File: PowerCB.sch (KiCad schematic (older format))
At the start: 16 parts, among them J1 USB_B_Micro, J2 Mounting_1, J3 Mounting_2, J6 Conn_01x02_Male, J7 Conn_01x02_Male, J8 Conn_01x02_Male, J9 Conn_01x02_Male, U1 TPS73633DBV

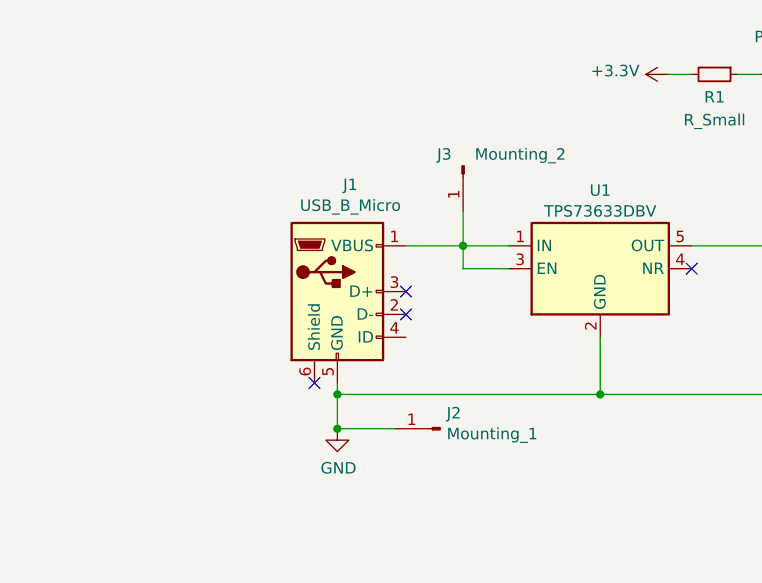
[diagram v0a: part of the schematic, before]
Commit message: feat: USB-C instead of Micro-USB connector
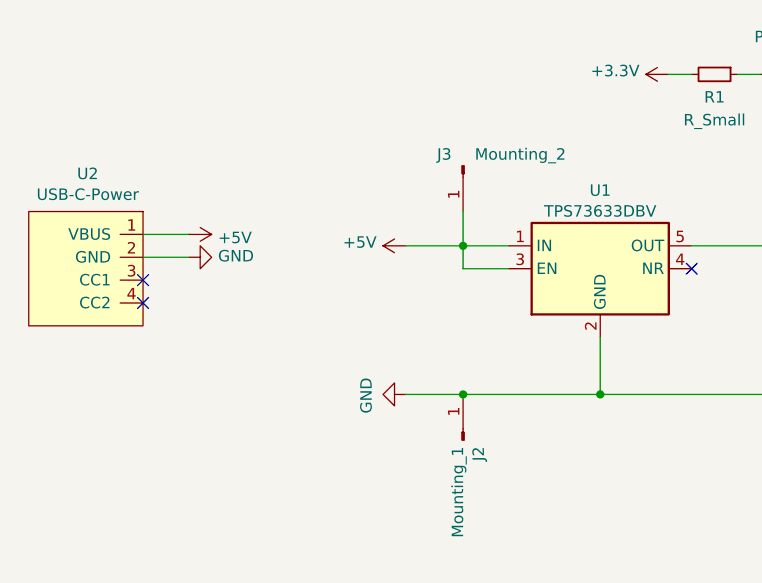
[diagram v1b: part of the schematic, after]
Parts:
- removed J1: USB_B_Micro, Connector_USB:USB_Micro-B_Amphenol_10103594-0001LF_Horizontal, symbol Connector:USB_B_Micro
- added U2: USB-C-Power, PowerCB:UJC-HP-3-SMT-TR, symbol PowerCB:USB-C-Power
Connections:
- net GND: now also U2.2 (GND)
- net +5V: now reaches J3.1 (Pin_1), U1.1 (IN), U1.3 (EN)
- net +5V: now also U2.1 (VBUS)
- no-connect marks 4 -> 3
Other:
- moved on the sheet: J2
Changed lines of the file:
@@
 EESchema Schematic File Version 4
-LIBS:PowerCB-cache
 EELAYER 30 0
 EELAYER END
@@
 Sheet 1 1
 Title "PowerCB"
-Date "2019-12-01"
-Rev "1.0"
+Date "2020-12-11"
+Rev "02"
 Comp ""
 Comment1 "https://creativecommons.org/licenses/by/4.0/"
@@
 Wire Wire Line
 	2800 2050 3000 2050
-NoConn ~ 2550 2250
-NoConn ~ 2550 2350
-Wire Wire Line
-	2250 2650 2250 2700
 $Comp
 L Device:LED D1
@@
 	4400 1300 4500 1300
 Wire Wire Line
-	3400 2700 2250 2700
-Wire Wire Line
 	3400 2450 3400 2700
-Connection ~ 2250 2700
-$Comp
-L Connector:USB_B_Micro J1
-U 1 1 5DA6372D
-P 2250 2250
-F 0 "J1" H 2307 2717 50  0000 C CNN
-F 1 "USB_B_Micro" H 2307 2626 50  0000 C CNN
-F 2 "Connector_USB:USB_Micro-B_Amphenol_10103594-0001LF_Horizontal" H 2400 2200 50  0001 C CNN
-F 3 "~" H 2400 2200 50  0001 C CNN
-	1    2250 2250
-	1    0    0    -1
-$EndComp
 $Comp
 L Connector:Conn_01x01_Male J3
@@
 Wire Wire Line
 	6950 3250 6650 3250
-NoConn ~ 2150 2650
+NoConn ~ 1400 2200
 $Comp
 L power:GND #PWR01
 U 1 1 5D9772CB
-P 2250 2850
-F 0 "#PWR01" H 2250 2600 50  0001 C CNN
-F 1 "GND" H 2255 2677 50  0000 C CNN
-F 2 "" H 2250 2850 50  0001 C CNN
-F 3 "" H 2250 2850 50  0001 C CNN
-	1    2250 2850
-	1    0    0    -1
+P 2550 2700
+F 0 "#PWR01" H 2550 2450 50  0001 C CNN
+F 1 "GND" H 2555 2527 50  0000 C CNN
+F 2 "" H 2550 2700 50  0001 C CNN
+F 3 "" H 2550 2700 50  0001 C CNN
+	1    2550 2700
+	0    1    1    0
 $EndComp
 $Comp
 L Connector:Conn_01x01_Male J2
 U 1 1 5DA96406
-P 2700 2850
-F 0 "J2" H 2672 2782 50  0000 R CNN
-F 1 "Mounting_1" H 2672 2873 50  0000 R CNN
-F 2 "MountingHole:MountingHole_2.2mm_M2_DIN965_Pad" H 2700 2850 50  0001 C CNN
-F 3 "~" H 2700 2850 50  0001 C CNN
-	1    2700 2850
-	-1   0    0    1
-$EndComp
-Wire Wire Line
-	2250 2700 2250 2850
-Wire Wire Line
-	2250 2850 2500 2850
-Connection ~ 2250 2850
+P 2800 2900
+F 0 "J2" H 2772 2832 50  0000 R CNN
+F 1 "Mounting_1" H 2772 2923 50  0000 R CNN
+F 2 "MountingHole:MountingHole_2.2mm_M2_DIN965_Pad" H 2800 2900 50  0001 C CNN
+F 3 "~" H 2800 2900 50  0001 C CNN
+	1    2800 2900
+	0    -1   -1   0
+$EndComp
 Wire Wire Line
 	2800 1900 2800 2050
@@
 	4350 2700 4550 2700
 Wire Wire Line
-	3400 2700 4350 2700
-Wire Wire Line
 	3800 2050 4350 2050
 Wire Wire Line
@@
 	5350 2050 5500 2050
 Connection ~ 5350 2050
+Wire Wire Line
+	3400 2700 2800 2700
+Wire Wire Line
+	3400 2700 4350 2700
+$Comp
+L PowerCB:USB-C-Power U2
+U 1 1 5FD43F49
+P 1150 2150
+F 0 "U2" H 1158 2565 50  0000 C CNN
+F 1 "USB-C-Power" H 1158 2474 50  0000 C CNN
+F 2 "PowerCB:UJC-HP-3-SMT-TR" H 1100 2450 50  0001 C CNN
+F 3 "" H 1100 2450 50  0001 C CNN
+	1    1150 2150
+	1    0    0    -1
+$EndComp
+NoConn ~ 1400 2300
+$Comp
+L power:+5V #PWR?
+U 1 1 5FD3C1AD
+P 1600 2000
+F 0 "#PWR?" H 1600 1850 50  0001 C CNN
+F 1 "+5V" V 1615 2128 50  0000 L CNN
+F 2 "" H 1600 2000 50  0001 C CNN
+F 3 "" H 1600 2000 50  0001 C CNN
+	1    1600 2000
+	0    1    1    0
+$EndComp
+$Comp
+L power:GND #PWR?
+U 1 1 5FD3CA40
+P 1600 2100
+F 0 "#PWR?" H 1600 1850 50  0001 C CNN
+F 1 "GND" V 1605 1972 50  0000 R CNN
+F 2 "" H 1600 2100 50  0001 C CNN
+F 3 "" H 1600 2100 50  0001 C CNN
+	1    1600 2100
+	0    -1   -1   0
+$EndComp
+Wire Wire Line
+	1400 2100 1600 2100
+Wire Wire Line
+	1600 2000 1400 2000
+$Comp
+L power:+5V #PWR?
+U 1 1 5FD407E4
+P 2550 2050
+F 0 "#PWR?" H 2550 1900 50  0001 C CNN
+F 1 "+5V" V 2565 2178 50  0000 L CNN
+F 2 "" H 2550 2050 50  0001 C CNN
+F 3 "" H 2550 2050 50  0001 C CNN
+	1    2550 2050
+	0    -1   -1   0
+$EndComp
+Connection ~ 2800 2700
+Wire Wire Line
+	2550 2700 2800 2700
 $EndSCHEMATC
